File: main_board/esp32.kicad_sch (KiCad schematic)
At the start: 8 parts, among them J2 Micro_SD_Card_Det_Hirose_DM3AT, U2 MCP1700x-330xxTT

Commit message: started adding main board
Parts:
- removed C9: 0.1U, Capacitor_SMD:C_0805_2012Metric_Pad1.18x1.45mm_HandSolder, symbol Device:C
- removed ESP32_1: ESP32_Devkit_DOIT_V1, footprints:ESP32_Devkit_DOIT_V1, symbol firestarter_library:ESP32_Devkit_DOIT_V1
- removed J2: Micro_SD_Card_Det_Hirose_DM3AT, footprints:microSD_HC_Hirose_DM3AT-SF-PEJM5, symbol Connector:Micro_SD_Card_Det_Hirose_DM3AT
- removed R4, R5, R6, R7: 10K, Resistor_SMD:R_0805_2012Metric, symbol Device:R
- removed U2: MCP1700x-330xxTT, Package_TO_SOT_SMD:SOT-23, symbol Regulator_Linear:MCP1700x-330xxTT
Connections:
- no-connect marks 6 -> 0
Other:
- note removed: "details see https://www.mischianti.org/2021/02/17/doit-esp32-dev-kit-v1-high-resolution-pinout-and-specs/ the top four left pins are input only!"
- note removed: "https://hackaday.io/project/7651-heartbeat-logger/log/31967-hardware-storage https://nodemcu.readthedocs.io/en/release/sdcard/"

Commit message: started changing main board
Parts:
- added C9: 1uF, Capacitor_SMD:C_0805_2012Metric_Pad1.18x1.45mm_HandSolder, symbol Device:C
- added R4: 10K, Resistor_SMD:R_0805_2012Metric, symbol Device:R
- added SW1: SW_Push_Open, footprints:SW_SPST_CK_KXT3, symbol Switch:SW_Push
- added U2: ESP32-S3-WROOM-2, footprints:ESP32-S3-WROOM-2, symbol Espressif:ESP32-S3-WROOM-2
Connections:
- new net: C9.1, R4.2, U2.3 (EN)
- new net: SW1.1, U2.27 (GPIO0/BOOT)
- new net +3.3V: R4.1, U2.2 (3V3)
- new net CFG_DONE: U2.37 (U0TXD/GPIO43/CLK_OUT1)
- new net CFG_RST: U2.36 (U0RXD/GPIO44/CLK_OUT2)
- new net D+: U2.14 (GPIO20/U1CTS/ADC2_CH9/CLK_OUT1/USB_D+)
- new net D-: U2.13 (GPIO19/U1RTS/ADC2_CH8/CLK_OUT2/USB_D-)
- new net FREE: U2.10 (GPIO17/U1TXD/ADC2_CH6)
- new net GND: C9.2, SW1.2, U2.1 (GND), U2.40 (GND), U2.41 (GND)
- new net POT_SCL: U2.17 (GPIO9/TOUCH9/ADC1_CH8/FSPIHD/SUBSPIHD)
- new net POT_SDA: U2.12 (GPIO8/TOUCH8/ADC1_CH7/SUBSPICS1)
- new net SPI_SCK: U2.20 (GPIO12/TOUCH12/ADC2_CH1/FSPICLK/FSPIIO6/SUBSPICLK)
- new net SPI_SI: U2.19 (GPIO11/TOUCH11/ADC2_CH0/FSPID/FSPIIO5/SUBSPID)
- new net SPI_SO: U2.21 (GPIO13/TOUCH13/ADC2_CH2/FSPIQ/FSPIIO7/SUBSPIQ)
- new net SPI_SS: U2.18 (GPIO10/TOUCH10/ADC1_CH9/FSPICS0/FSPIIO4/SUBSPICS0)
- new net SPI_SS2: U2.22 (GPIO14/TOUCH14/ADC2_CH3/FSPIWP/FSPIDQS/SUBSPIWP)
- new net SPI_SS3: U2.35 (MTMS/GPIO42)
- new net STEP_ENABLE: U2.32 (MTCK/GPIO39/CLK_OUT3/SUBSPICS1)
- no-connect marks 0 -> 18
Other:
- note added: "ESP32"
- note added: "pinout is described here https://doc.riot-os.org/group__boards__esp32s3__devkit.html"

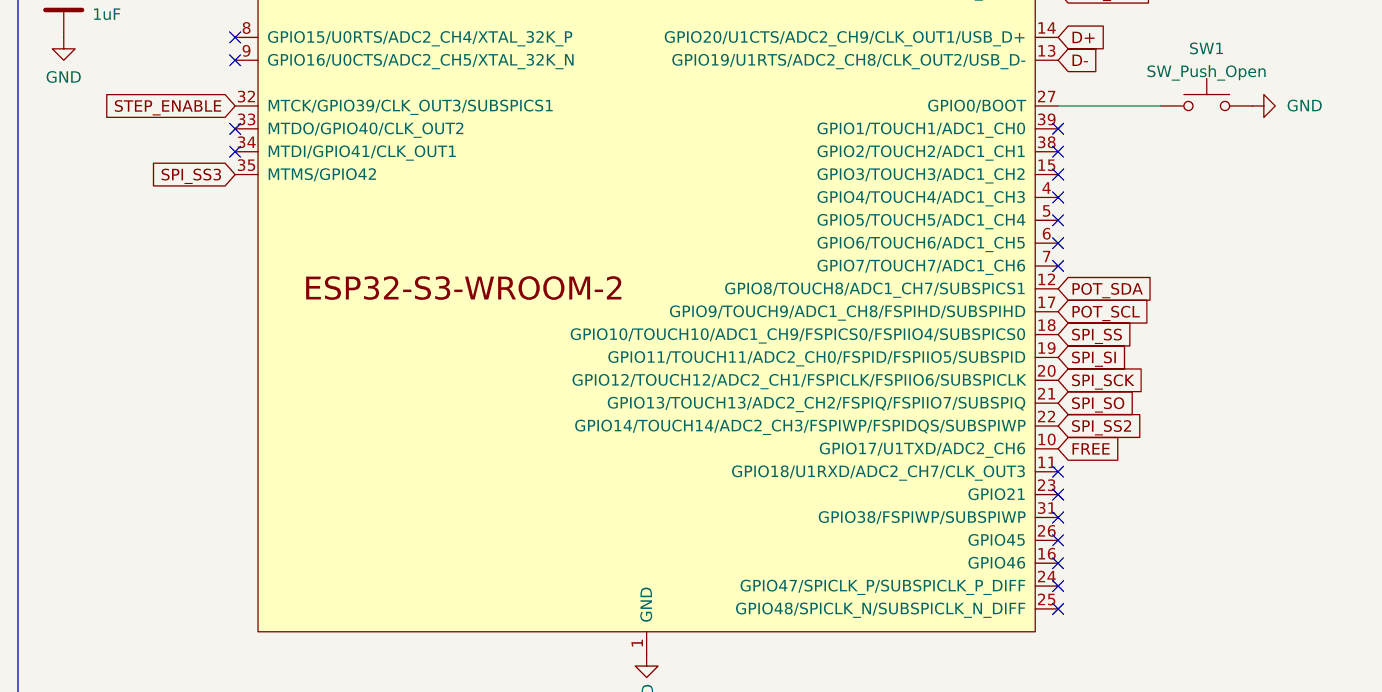
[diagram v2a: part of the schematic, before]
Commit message: updated step models
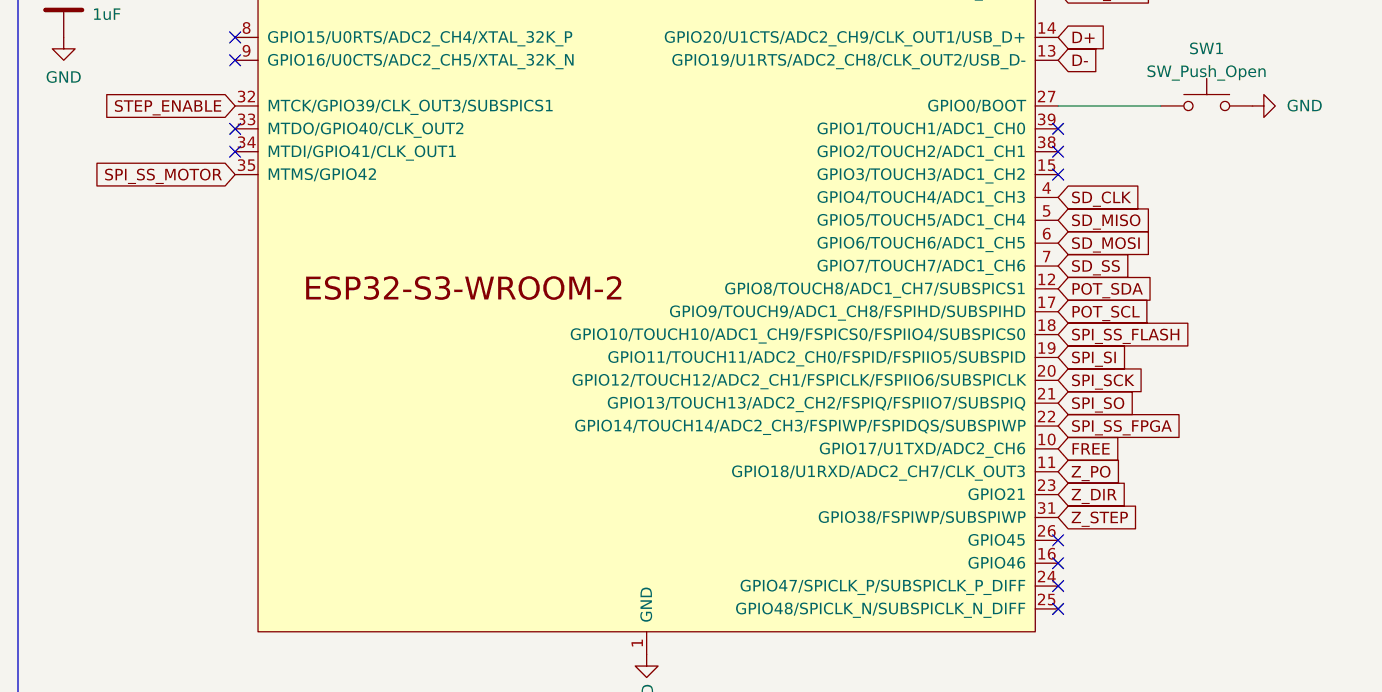
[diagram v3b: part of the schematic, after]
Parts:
- SW1: Farnell (none) -> 3023200
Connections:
- net Z_PO: now reaches U2.11 (GPIO18/U1RXD/ADC2_CH7/CLK_OUT3)
- net Z_DIR: now reaches U2.23 (GPIO21)
- net Z_STEP: now reaches U2.31 (GPIO38/FSPIWP/SUBSPIWP)
- net SD_CLK: now reaches U2.4 (GPIO4/TOUCH4/ADC1_CH3)
- net SD_MISO: now reaches U2.5 (GPIO5/TOUCH5/ADC1_CH4)
- net SD_MOSI: now reaches U2.6 (GPIO6/TOUCH6/ADC1_CH5)
- net SD_SS: now reaches U2.7 (GPIO7/TOUCH7/ADC1_CH6)
- net SPI_SS renamed SPI_SS_FLASH
- net SPI_SS2 renamed SPI_SS_FPGA
- net SPI_SS3 renamed SPI_SS_MOTOR
- no-connect marks 18 -> 11
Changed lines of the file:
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@@
   )
   (no_connect (at 200.66 85.09))
-  (no_connect (at 200.66 120.65))
   (no_connect (at 200.66 133.35))
   (no_connect (at 200.66 125.73))
   (no_connect (at 109.22 80.01))
   (no_connect (at 200.66 130.81))
-  (no_connect (at 200.66 87.63))
   (no_connect (at 200.66 82.55))
   (no_connect (at 200.66 80.01))
-  (no_connect (at 200.66 95.25))
-  (no_connect (at 200.66 90.17))
   (no_connect (at 109.22 82.55))
   (no_connect (at 109.22 69.85))
   (no_connect (at 200.66 128.27))
   (no_connect (at 109.22 72.39))
-  (no_connect (at 200.66 118.11))
-  (no_connect (at 200.66 92.71))
-  (no_connect (at 200.66 123.19))
   (wire (pts (xy 90.17 62.23) (xy 109.22 62.23))
     (stroke (width 0) (type default))
@@
     (effects (font (size 1.27 1.27)) (justify left bottom))
   )
-  (global_label "SPI_SS2" (shape input) (at 200.66 113.03 0) (fields_autoplaced)
-    (effects (font (size 1.27 1.27)) (justify left))
-    (property "Intersheetrefs" "${INTERSHEET_REFS}" (at 210.592 113.03 0)
+  (global_label "SPI_SS_FPGA" (shape input) (at 200.66 113.03 0) (fields_autoplaced)
+    (effects (font (size 1.27 1.27)) (justify left))
+    (property "Intersheetrefs" "${INTERSHEET_REFS}" (at 215.0673 113.03 0)
+      (effects (font (size 1.27 1.27)) (justify left) hide)
+    )
+  )
+  (global_label "SD_MOSI" (shape input) (at 200.66 92.71 0) (fields_autoplaced)
+    (effects (font (size 1.27 1.27)) (justify left))
+    (property "Intersheetrefs" "${INTERSHEET_REFS}" (at 210.9549 92.71 0)
       (effects (font (size 1.27 1.27)) (justify left) hide)
     )
@@
     (effects (font (size 1.27 1.27)) (justify left))
     (property "Intersheetrefs" "${INTERSHEET_REFS}" (at 210.9549 100.33 0)
+      (effects (font (size 1.27 1.27)) (justify left) hide)
+    )
+  )
+  (global_label "Z_STEP" (shape input) (at 200.66 123.19 0) (fields_autoplaced)
+    (effects (font (size 1.27 1.27)) (justify left))
+    (property "Intersheetrefs" "${INTERSHEET_REFS}" (at 209.6848 123.19 0)
       (effects (font (size 1.27 1.27)) (justify left) hide)
     )
@@
     )
   )
+  (global_label "Z_DIR" (shape input) (at 200.66 120.65 0) (fields_autoplaced)
+    (effects (font (size 1.27 1.27)) (justify left))
+    (property "Intersheetrefs" "${INTERSHEET_REFS}" (at 208.2335 120.65 0)
+      (effects (font (size 1.27 1.27)) (justify left) hide)
+    )
+  )
   (global_label "POT_SDA" (shape input) (at 200.66 97.79 0) (fields_autoplaced)
     (effects (font (size 1.27 1.27)) (justify left))
@@
     )
   )
-  (global_label "SPI_SS3" (shape input) (at 109.22 85.09 180)
+  (global_label "SPI_SS_MOTOR" (shape input) (at 109.22 85.09 180)
     (effects (font (size 1.27 1.27)) (justify right))
     (property "Intersheetrefs" "${INTERSHEET_REFS}" (at 109.22 85.09 0)
@@
     )
   )
-  (global_label "SPI_SS" (shape input) (at 200.66 102.87 0) (fields_autoplaced)
-    (effects (font (size 1.27 1.27)) (justify left))
-    (property "Intersheetrefs" "${INTERSHEET_REFS}" (at 209.3825 102.87 0)
+  (global_label "SPI_SS_FLASH" (shape input) (at 200.66 102.87 0) (fields_autoplaced)
+    (effects (font (size 1.27 1.27)) (justify left))
+    (property "Intersheetrefs" "${INTERSHEET_REFS}" (at 216.0954 102.87 0)
       (effects (font (size 1.27 1.27)) (justify left) hide)
     )
@@
     )
   )
+  (global_label "SD_CLK" (shape input) (at 200.66 87.63 0) (fields_autoplaced)
+    (effects (font (size 1.27 1.27)) (justify left))
+    (property "Intersheetrefs" "${INTERSHEET_REFS}" (at 209.9268 87.63 0)
+      (effects (font (size 1.27 1.27)) (justify left) hide)
+    )
+  )
+  (global_label "SD_MISO" (shape input) (at 200.66 90.17 0) (fields_autoplaced)
+    (effects (font (size 1.27 1.27)) (justify left))
+    (property "Intersheetrefs" "${INTERSHEET_REFS}" (at 210.9549 90.17 0)
+      (effects (font (size 1.27 1.27)) (justify left) hide)
+    )
+  )
   (global_label "D-" (shape input) (at 200.66 72.39 0) (fields_autoplaced)
     (effects (font (size 1.27 1.27)) (justify left))
@@
     )
   )
+  (global_label "SD_SS" (shape input) (at 200.66 95.25 0) (fields_autoplaced)
+    (effects (font (size 1.27 1.27)) (justify left))
+    (property "Intersheetrefs" "${INTERSHEET_REFS}" (at 208.7777 95.25 0)
+      (effects (font (size 1.27 1.27)) (justify left) hide)
+    )
+  )
   (global_label "D+" (shape input) (at 200.66 69.85 0) (fields_autoplaced)
     (effects (font (size 1.27 1.27)) (justify left))
     (property "Intersheetrefs" "${INTERSHEET_REFS}" (at 205.754 69.85 0)
+      (effects (font (size 1.27 1.27)) (justify left) hide)
+    )
+  )
+  (global_label "Z_PO" (shape input) (at 200.66 118.11 0) (fields_autoplaced)
+    (effects (font (size 1.27 1.27)) (justify left))
+    (property "Intersheetrefs" "${INTERSHEET_REFS}" (at 207.6892 118.11 0)
       (effects (font (size 1.27 1.27)) (justify left) hide)
     )
@@
       (effects (font (size 1.27 1.27)) hide)
     )
-    (property "Datasheet" "~" (at 217.17 72.39 0)
-      (effects (font (size 1.27 1.27)) hide)
-    )
+    (property "Datasheet" "https://nl.farnell.com/c-k-components/kxt-331-lhs/tactile-switch-spst-0-02a-15vdc/dp/3023200?st=kxt3" (at 217.17 72.39 0)
+      (effects (font (size 1.27 1.27)) hide)
+    )
+    (property "Farnell" "3023200" (at 217.17 77.47 0)
+      (effects (font (size 1.27 1.27)) hide)
+    )

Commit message: routed main board
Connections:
- net CFG_DONE: now also U2.31 (GPIO38/FSPIWP/SUBSPIWP); no longer U2.37 (U0TXD/GPIO43/CLK_OUT1)
- net CFG_RST: now also U2.24 (GPIO47/SPICLK_P/SUBSPICLK_P_DIFF); no longer U2.36 (U0RXD/GPIO44/CLK_OUT2)
- net FREE: now also U2.32 (MTCK/GPIO39/CLK_OUT3/SUBSPICS1); no longer U2.10 (GPIO17/U1TXD/ADC2_CH6)
- net POT_SCL: now also U2.18 (GPIO10/TOUCH10/ADC1_CH9/FSPICS0/FSPIIO4/SUBSPICS0); no longer U2.17 (GPIO9/TOUCH9/ADC1_CH8/FSPIHD/SUBSPIHD)
- net POT_SDA: now also U2.25 (GPIO48/SPICLK_N/SUBSPICLK_N_DIFF); no longer U2.12 (GPIO8/TOUCH8/ADC1_CH7/SUBSPICS1)
- net SPI_SS_FLASH: now also U2.33 (MTDO/GPIO40/CLK_OUT2); no longer U2.18 (GPIO10/TOUCH10/ADC1_CH9/FSPICS0/FSPIIO4/SUBSPICS0)
- net SPI_SS_FPGA: now also U2.26 (GPIO45); no longer U2.22 (GPIO14/TOUCH14/ADC2_CH3/FSPIWP/FSPIDQS/SUBSPIWP)
- net STEP_ENABLE: now also U2.17 (GPIO9/TOUCH9/ADC1_CH8/FSPIHD/SUBSPIHD); no longer U2.32 (MTCK/GPIO39/CLK_OUT3/SUBSPICS1)
- net Z_STEP: now also U2.37 (U0TXD/GPIO43/CLK_OUT1); no longer U2.31 (GPIO38/FSPIWP/SUBSPIWP)
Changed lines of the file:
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@@
   )
   (no_connect (at 200.66 85.09))
-  (no_connect (at 200.66 133.35))
-  (no_connect (at 200.66 125.73))
-  (no_connect (at 109.22 80.01))
-  (no_connect (at 200.66 130.81))
+  (no_connect (at 200.66 97.79))
+  (no_connect (at 200.66 113.03))
+  (no_connect (at 200.66 64.77))
   (no_connect (at 200.66 82.55))
   (no_connect (at 200.66 80.01))
@@
   (no_connect (at 200.66 128.27))
   (no_connect (at 109.22 72.39))
+  (no_connect (at 200.66 115.57))
   (wire (pts (xy 90.17 62.23) (xy 109.22 62.23))
     (stroke (width 0) (type default))
@@
     (effects (font (size 1.27 1.27)) (justify left bottom))
   )
-  (global_label "SPI_SS_FPGA" (shape input) (at 200.66 113.03 0) (fields_autoplaced)
+  (global_label "SPI_SS_FPGA" (shape input) (at 200.66 125.73 0) (fields_autoplaced)
     (effects (font (size 1.27 1.27)) (justify left))
-    (property "Intersheetrefs" "${INTERSHEET_REFS}" (at 215.0673 113.03 0)
+    (property "Intersheetrefs" "${INTERSHEET_REFS}" (at 215.0673 125.73 0)
       (effects (font (size 1.27 1.27)) (justify left) hide)
     )
@@
     )
   )
-  (global_label "POT_SCL" (shape input) (at 200.66 100.33 0) (fields_autoplaced)
+  (global_label "POT_SCL" (shape input) (at 200.66 102.87 0) (fields_autoplaced)
     (effects (font (size 1.27 1.27)) (justify left))
-    (property "Intersheetrefs" "${INTERSHEET_REFS}" (at 210.9549 100.33 0)
+    (property "Intersheetrefs" "${INTERSHEET_REFS}" (at 210.9549 102.87 0)
       (effects (font (size 1.27 1.27)) (justify left) hide)
     )
   )
-  (global_label "Z_STEP" (shape input) (at 200.66 123.19 0) (fields_autoplaced)
+  (global_label "Z_STEP" (shape input) (at 200.66 62.23 0) (fields_autoplaced)
     (effects (font (size 1.27 1.27)) (justify left))
-    (property "Intersheetrefs" "${INTERSHEET_REFS}" (at 209.6848 123.19 0)
+    (property "Intersheetrefs" "${INTERSHEET_REFS}" (at 209.6848 62.23 0)
       (effects (font (size 1.27 1.27)) (justify left) hide)
     )
   )
-  (global_label "STEP_ENABLE" (shape input) (at 109.22 77.47 180)
-    (effects (font (size 1.27 1.27)) (justify right))
-    (property "Intersheetrefs" "${INTERSHEET_REFS}" (at 109.22 77.47 0)
+  (global_label "STEP_ENABLE" (shape input) (at 200.66 100.33 0)
+    (effects (font (size 1.27 1.27)) (justify left))
+    (property "Intersheetrefs" "${INTERSHEET_REFS}" (at 200.66 100.33 0)
       (effects (font (size 1.27 1.27)) hide)
     )
@@
     )
   )
-  (global_label "POT_SDA" (shape input) (at 200.66 97.79 0) (fields_autoplaced)
+  (global_label "POT_SDA" (shape input) (at 200.66 133.35 0) (fields_autoplaced)
     (effects (font (size 1.27 1.27)) (justify left))
-    (property "Intersheetrefs" "${INTERSHEET_REFS}" (at 211.0154 97.79 0)
+    (property "Intersheetrefs" "${INTERSHEET_REFS}" (at 211.0154 133.35 0)
       (effects (font (size 1.27 1.27)) (justify left) hide)
     )
@@
     )
   )
-  (global_label "SPI_SS_FLASH" (shape input) (at 200.66 102.87 0) (fields_autoplaced)
-    (effects (font (size 1.27 1.27)) (justify left))
-    (property "Intersheetrefs" "${INTERSHEET_REFS}" (at 216.0954 102.87 0)
-      (effects (font (size 1.27 1.27)) (justify left) hide)
+  (global_label "SPI_SS_FLASH" (shape input) (at 109.22 80.01 180) (fields_autoplaced)
+    (effects (font (size 1.27 1.27)) (justify right))
+    (property "Intersheetrefs" "${INTERSHEET_REFS}" (at 93.7846 80.01 0)
+      (effects (font (size 1.27 1.27)) (justify right) hide)
     )
   )
-  (global_label "FREE" (shape input) (at 200.66 115.57 0) (fields_autoplaced)
-    (effects (font (size 1.27 1.27)) (justify left))
-    (property "Intersheetrefs" "${INTERSHEET_REFS}" (at 207.5682 115.57 0)
-      (effects (font (size 1.27 1.27)) (justify left) hide)
+  (global_label "FREE" (shape input) (at 109.22 77.47 180) (fields_autoplaced)
+    (effects (font (size 1.27 1.27)) (justify right))
+    (property "Intersheetrefs" "${INTERSHEET_REFS}" (at 102.3118 77.47 0)
+      (effects (font (size 1.27 1.27)) (justify right) hide)
     )
   )
@@
     )
   )
-  (global_label "CFG_RST" (shape input) (at 200.66 64.77 0) (fields_autoplaced)
+  (global_label "CFG_RST" (shape input) (at 200.66 130.81 0) (fields_autoplaced)
     (effects (font (size 1.27 1.27)) (justify left))
-    (property "Intersheetrefs" "${INTERSHEET_REFS}" (at 210.9549 64.77 0)
+    (property "Intersheetrefs" "${INTERSHEET_REFS}" (at 210.9549 130.81 0)
       (effects (font (size 1.27 1.27)) (justify left) hide)
     )
@@
     )
   )
-  (global_label "CFG_DONE" (shape input) (at 200.66 62.23 0) (fields_autoplaced)
+  (global_label "CFG_DONE" (shape input) (at 200.66 123.19 0) (fields_autoplaced)
     (effects (font (size 1.27 1.27)) (justify left))
-    (property "Intersheetrefs" "${INTERSHEET_REFS}" (at 212.5878 62.23 0)
+    (property "Intersheetrefs" "${INTERSHEET_REFS}" (at 212.5878 123.19 0)
       (effects (font (size 1.27 1.27)) (justify left) hide)
     )
